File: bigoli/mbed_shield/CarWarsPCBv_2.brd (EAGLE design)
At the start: 68.6 x 55.9 mm, 22 parts, among them J1 MAGJACK, Q1 220mA/50V/3.5Ω, Q2 220mA/50V/3.5Ω

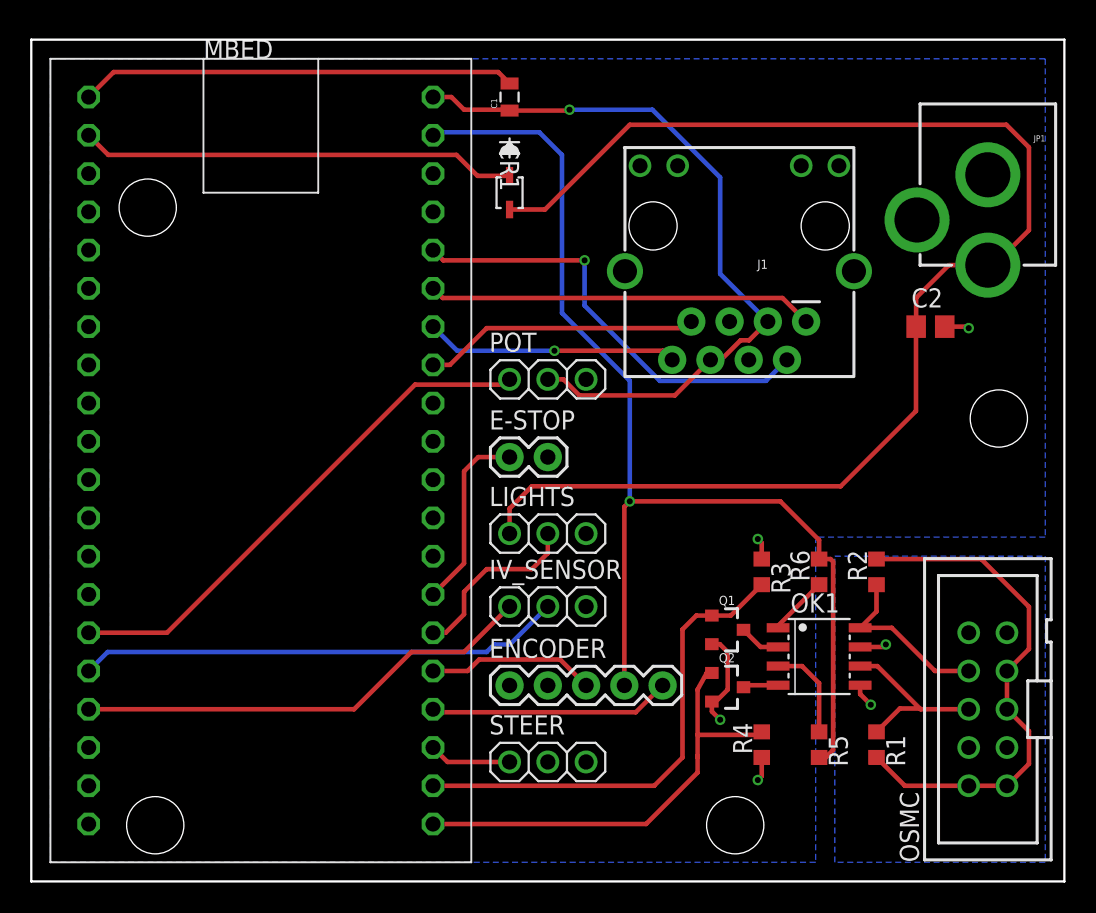
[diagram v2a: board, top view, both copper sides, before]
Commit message: Added corrected spec-ed capacitor and resistor for neopixel
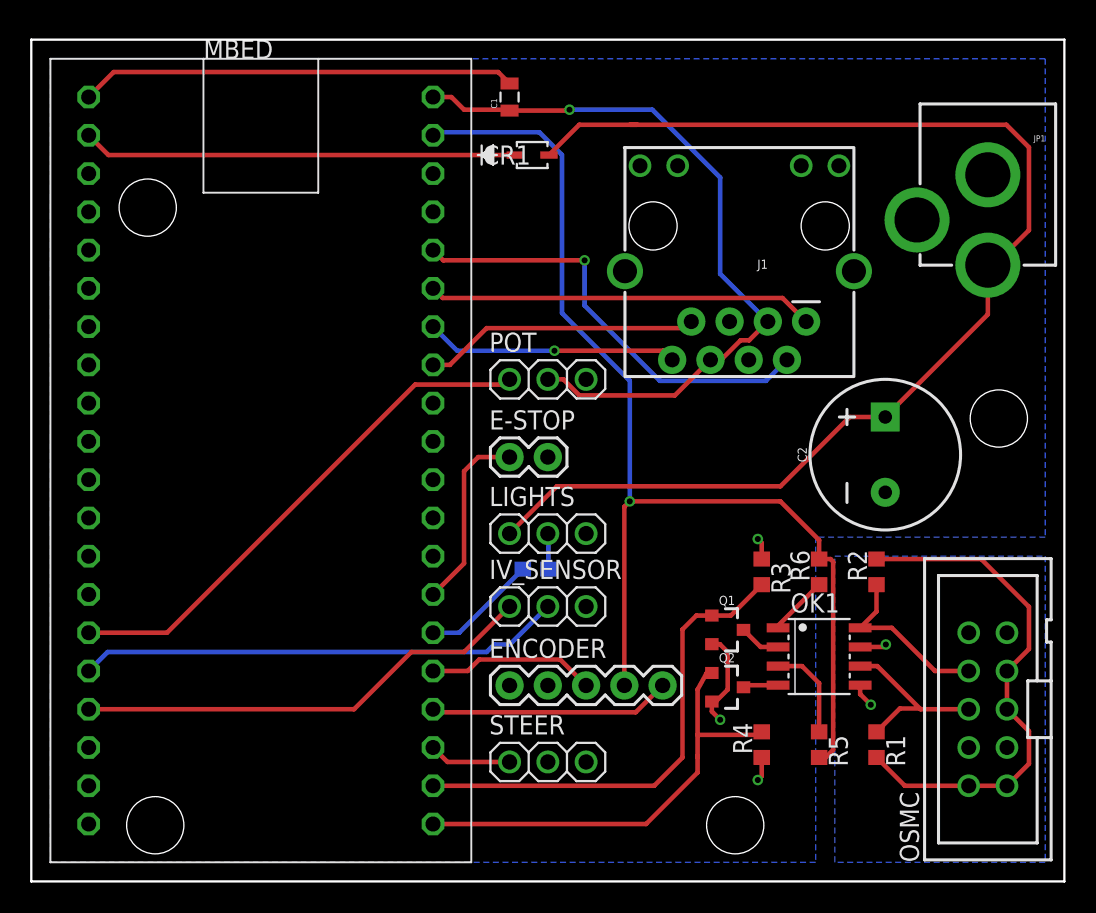
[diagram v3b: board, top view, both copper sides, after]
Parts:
- added R7: 340, SparkFun-Resistors:0603
- C2: value 1000PF -> 1mf; device rcl:C0805 -> SparkFun-Capacitors:CPOL-RADIAL-5MM-10MM-KIT
- moved C2 9.01 mm to (58.0, 29.6), turned to 90 degrees
- moved CR1 2.92 mm to (34.5, 49.5), turned to 0 degrees
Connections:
- net N$1 renamed VIN
- new net N$6: LIGHTS.2, R7.2
- net GND: now also C2.-; no longer C2.2
- net NEOPIXEL_CONTROL: now also R7.1; no longer LIGHTS.2
- net VCC: now also C2.+; no longer C2.1
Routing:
- net VCC: track 91.2 -> 84.1 mm
- net NEOPIXEL_CONTROL: track 12.0 -> 7.71 mm
- net N$6: track 0.00 -> 2.38 mm
- net GND: track 40.2 -> 38.6 mm, vias 4 -> 3
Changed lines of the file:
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@@
 <elements>
 <element name="C1" library="SparkFun-Capacitors" package="0805" value="0.1uF" x="33.02" y="53.34" rot="R90"/>
-<element name="CR1" library="Digikey" package="SOD-323" value="BAT60JFILM" x="33.02" y="46.99" rot="R270">
-<attribute name="MANUFACTURER_PART_NUMBER" value="BAT60JFILM" x="33.02" y="46.99" size="1.778" layer="27" rot="R270" display="off"/>
-<attribute name="VENDOR" value="ST Microelectronics" x="33.02" y="46.99" size="1.778" layer="27" rot="R270" display="off"/>
+<element name="CR1" library="Digikey" package="SOD-323" value="BAT60JFILM" x="34.52" y="49.49">
+<attribute name="MANUFACTURER_PART_NUMBER" value="BAT60JFILM" x="34.52" y="49.49" size="1.778" layer="27" display="off"/>
+<attribute name="VENDOR" value="ST Microelectronics" x="34.52" y="49.49" size="1.778" layer="27" display="off"/>
 </element>
 <element name="E-STOP" library="SparkFun-Connectors" package="1X02" value="" x="33.02" y="29.44"/>
@@
 <element name="R6" library="rcl" library_urn="urn:adsk.eagle:library:334" package="R0603" value="1K" x="53.57" y="21.82" rot="R90"/>
 <element name="STEER" library="Roboracing" package="1X03" value="" x="35.56" y="9.2"/>
-<element name="C2" library="rcl" library_urn="urn:adsk.eagle:library:334" package="C0805" value="1000PF" x="60.96" y="38.1"/>
+<element name="C2" library="SparkFun-Capacitors" library_urn="urn:adsk.eagle:library:510" package="CPOL-RADIAL-5MM-10MM-KIT" package3d_urn="urn:adsk.eagle:package:37421/1" value="1mf" x="57.96" y="29.6" rot="R90">
+<attribute name="PROD_ID" value="CAP-09538" x="57.96" y="29.6" size="1.778" layer="27" rot="R90" display="off"/>
+<attribute name="VALUE" value="1mf" x="57.96" y="29.6" size="1.778" layer="27" rot="R90" display="off"/>
+</element>
+<element name="R7" library="SparkFun-Resistors" library_urn="urn:adsk.eagle:library:532" package="0603" package3d_urn="urn:adsk.eagle:package:39650/1" value="340" x="34.75" y="22" rot="MR180">
+<attribute name="PROD_ID" value="RES-12616" x="34.75" y="22" size="1.778" layer="28" rot="MR180" display="off"/>
+</element>
 </elements>
 <signals>
@@
 <contactref element="Q1" pad="2"/>
 <contactref element="R3" pad="1"/>
-<contactref element="C2" pad="2"/>
+<contactref element="C2" pad="-"/>
 <polygon width="0.1524" layer="16">
 <vertex x="2.54" y="55.88"/>
@@
 <vertex x="2.54" y="2.54"/>
 </polygon>
-<wire x1="61.91" y1="38.1" x2="63.4" y2="38.1" width="0.3048" layer="1"/>
-<wire x1="63.4" y1="38.1" x2="63.5" y2="38" width="0.3048" layer="1"/>
-<via x="63.5" y="38" extent="1-16" drill="0.4"/>
 <wire x1="49.76" y1="22.67" x2="49.76" y2="23.74" width="0.3048" layer="1"/>
 <wire x1="49.76" y1="23.74" x2="49.5" y2="24" width="0.3048" layer="1"/>
@@
 </signal>
 <signal name="NEOPIXEL_CONTROL">
-<contactref element="LIGHTS" pad="2"/>
 <contactref element="MBED" pad="26"/>
-<wire x1="35.56" y1="24.36" x2="35.56" y2="23.06" width="0.3048" layer="1"/>
-<wire x1="35.56" y1="23.06" x2="34.5" y2="22" width="0.3048" layer="1"/>
-<wire x1="34.5" y1="22" x2="31.5" y2="22" width="0.3048" layer="1"/>
-<wire x1="31.5" y1="22" x2="30" y2="20.5" width="0.3048" layer="1"/>
-<wire x1="30" y1="20.5" x2="30" y2="19" width="0.3048" layer="1"/>
-<wire x1="28.78" y1="17.78" x2="27.94" y2="17.78" width="0.3048" layer="1"/>
-<wire x1="30" y1="19" x2="28.78" y2="17.78" width="0.3048" layer="1"/>
+<contactref element="R7" pad="1"/>
+<wire x1="27.94" y1="17.78" x2="29.68" y2="17.78" width="0.3048" layer="16"/>
+<wire x1="29.68" y1="17.78" x2="33.9" y2="22" width="0.3048" layer="16"/>
 </signal>
 <signal name="E-STOP_STATUS">
@@
 <contactref element="LIGHTS" pad="1"/>
 <contactref element="CR1" pad="2"/>
-<contactref element="C2" pad="1"/>
-<wire x1="60.01" y1="38.191771875" x2="60.01" y2="40.01" width="0.3048" layer="1"/>
-<wire x1="60.01" y1="38.191771875" x2="60.01" y2="38.1" width="0.3048" layer="1"/>
-<wire x1="62.18" y1="42.18" x2="64.77" y2="42.18" width="0.3048" layer="1"/>
-<wire x1="60.01" y1="40.01" x2="62.18" y2="42.18" width="0.3048" layer="1"/>
-<wire x1="64.77" y1="42.18" x2="65.18" y2="42.18" width="0.3048" layer="1"/>
+<contactref element="C2" pad="+"/>
+<wire x1="65.18" y1="42.18" x2="64.77" y2="42.18" width="0.3048" layer="1"/>
 <wire x1="65.18" y1="42.18" x2="67.5" y2="44.5" width="0.3048" layer="1"/>
 <wire x1="67.5" y1="44.5" x2="67.5" y2="50" width="0.3048" layer="1"/>
 <wire x1="67.5" y1="50" x2="66" y2="51.5" width="0.3048" layer="1"/>
-<wire x1="66" y1="51.5" x2="41" y2="51.5" width="0.3048" layer="1"/>
-<wire x1="35.3724" y1="45.8724" x2="33.02" y2="45.8724" width="0.3048" layer="1"/>
-<wire x1="41" y1="51.5" x2="35.3724" y2="45.8724" width="0.3048" layer="1"/>
-<wire x1="33.02" y1="24.36" x2="33.02" y2="26.02" width="0.3048" layer="1"/>
-<wire x1="33.02" y1="26.02" x2="34.5" y2="27.5" width="0.3048" layer="1"/>
-<wire x1="34.5" y1="27.5" x2="55" y2="27.5" width="0.3048" layer="1"/>
-<wire x1="55" y1="27.5" x2="60" y2="32.5" width="0.3048" layer="1"/>
-<wire x1="60" y1="32.5" x2="60" y2="38.181771875" width="0.3048" layer="1"/>
-<wire x1="60" y1="38.181771875" x2="60.01" y2="38.191771875" width="0.3048" layer="1"/>
+<wire x1="66" y1="51.5" x2="41.5" y2="51.5" width="0.3048" layer="1"/>
+<wire x1="41.5" y1="51.5" x2="41" y2="51.5" width="0.3048" layer="1"/>
+<wire x1="64.77" y1="42.18" x2="64.77" y2="38.91" width="0.3048" layer="1"/>
+<wire x1="64.77" y1="38.91" x2="57.96" y2="32.1" width="0.3048" layer="1"/>
+<wire x1="57.96" y1="32.1" x2="55.6" y2="32.1" width="0.3048" layer="1"/>
+<wire x1="55.6" y1="32.1" x2="51" y2="27.5" width="0.3048" layer="1"/>
+<wire x1="51" y1="27.5" x2="36.16" y2="27.5" width="0.3048" layer="1"/>
+<wire x1="36.16" y1="27.5" x2="33.02" y2="24.36" width="0.3048" layer="1"/>
+<wire x1="41.5" y1="51.5" x2="37.6476" y2="51.5" width="0.3048" layer="1"/>
+<wire x1="37.6476" y1="51.5" x2="35.6376" y2="49.49" width="0.3048" layer="1"/>
 </signal>
 <signal name="I_SENSE">
@@
 <wire x1="31.5" y1="16.5" x2="6.34" y2="16.5" width="0.3048" layer="16"/>
 </signal>
-<signal name="N$1">
+<signal name="VIN">
 <contactref element="MBED" pad="2"/>
 <contactref element="CR1" pad="1"/>
-<wire x1="33.02" y1="48.1076" x2="30.8924" y2="48.1076" width="0.3048" layer="1"/>
-<wire x1="30.8924" y1="48.1076" x2="29.5" y2="49.5" width="0.3048" layer="1"/>
-<wire x1="29.5" y1="49.5" x2="6.38" y2="49.5" width="0.3048" layer="1"/>
-<wire x1="6.38" y1="49.5" x2="5.08" y2="50.8" width="0.3048" layer="1"/>
+<wire x1="33.4024" y1="49.49" x2="6.39" y2="49.49" width="0.3048" layer="1"/>
+<wire x1="6.39" y1="49.49" x2="5.08" y2="50.8" width="0.3048" layer="1"/>
 </signal>
 <signal name="DGND">
@@
 <wire x1="50.8466" y1="18.2466" x2="50.8466" y2="18.105" width="0.3048" layer="1"/>
 </signal>
+<signal name="N$6">
+<contactref element="LIGHTS" pad="2"/>
+<contactref element="R7" pad="2"/>
+<wire x1="35.6" y1="22" x2="35.6" y2="24.32" width="0.3048" layer="16"/>
+<wire x1="35.6" y1="24.32" x2="35.56" y2="24.36" width="0.3048" layer="16"/>
+</signal>
 </signals>
 </board>
@@
 with this version.
 </note>
+<note version="8.3" severity="warning">
+Since Version 8.3, EAGLE supports URNs for individual library
+assets (packages, symbols, and devices). The URNs of those assets
+will not be understood (or retained) with this version.
+</note>
+<note version="8.3" severity="warning">
+Since Version 8.3, EAGLE supports the association of 3D packages
+with devices in libraries, schematics, and board files. Those 3D
+packages will not be understood (or retained) with this version.
+</note>
 </compatibility>
